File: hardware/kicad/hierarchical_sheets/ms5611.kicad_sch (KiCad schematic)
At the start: 3 parts, among them U4 MS5611-01BA

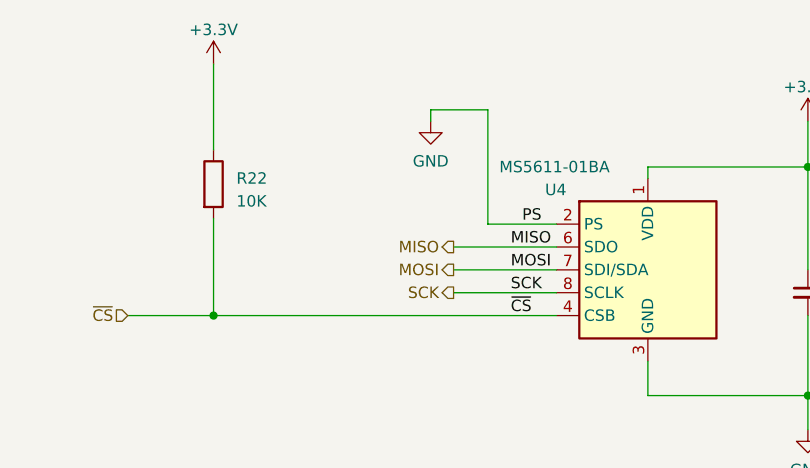
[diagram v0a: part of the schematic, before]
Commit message: assigned footprints
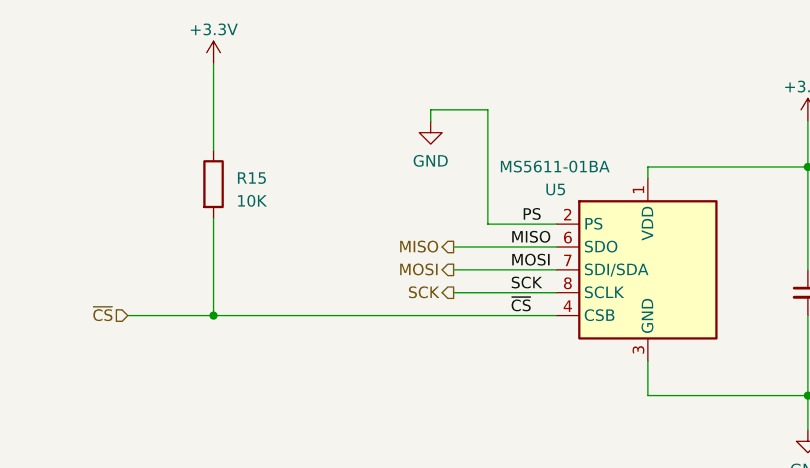
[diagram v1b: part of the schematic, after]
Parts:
- C6: footprint (none) -> Resistor_SMD:R_0603_1608Metric
- R15: renamed from R22; footprint (none) -> Resistor_SMD:R_0603_1608Metric
- U5: renamed from U4; Digikey https://www.digikey.com/en/products/detail/te-connectivity-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 -> (none)
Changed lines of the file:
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@@
         )
         (path "/54cce219-8b98-4e71-96c4-f9ee784aa3bc/01e59dc5-0a98-4437-b4f9-a1305517a629"
-          (reference "#PWR07") (unit 1)
+          (reference "#PWR024") (unit 1)
         )
       )
@@
   (symbol (lib_id "Device:R") (at 40.005 77.47 0) (unit 1)
     (in_bom yes) (on_board yes) (dnp no) (fields_autoplaced)
-    (property "Reference" "R22" (at 42.545 76.835 0)
+    (property "Reference" "R15" (at 42.545 76.835 0)
       (effects (font (size 1.27 1.27)) (justify left))
     )
@@
       (effects (font (size 1.27 1.27)) (justify left))
     )
-    (property "Footprint" "" (at 38.227 77.47 90)
+    (property "Footprint" "Resistor_SMD:R_0603_1608Metric" (at 38.227 77.47 90)
       (effects (font (size 1.27 1.27)) hide)
     )
@@
       (project "FC"
         (path "/54cce219-8b98-4e71-96c4-f9ee784aa3bc/01e59dc5-0a98-4437-b4f9-a1305517a629"
-          (reference "R22") (unit 1)
+          (reference "R15") (unit 1)
         )
       )
@@
         )
         (path "/54cce219-8b98-4e71-96c4-f9ee784aa3bc/01e59dc5-0a98-4437-b4f9-a1305517a629"
-          (reference "#PWR05") (unit 1)
+          (reference "#PWR023") (unit 1)
         )
       )
@@
   (symbol (lib_id "Sensor_Pressure:MS5611-01BA") (at 88.265 86.995 0) (unit 1)
     (in_bom yes) (on_board yes) (dnp no)
-    (property "Reference" "U4" (at 76.835 78.105 0)
+    (property "Reference" "U5" (at 76.835 78.105 0)
       (effects (font (size 1.27 1.27)) (justify left))
     )
@@
     )
     (property "Datasheet" "https://www.te.com/commerce/DocumentDelivery/DDEController?Action=srchrtrv&DocNm=MS5611-01BA03&DocType=Data+Sheet&DocLang=English" (at 88.265 86.995 0)
-      (effects (font (size 1.27 1.27)) hide)
-    )
-    (property "Digikey" "https://www.digikey.com/en/products/detail/te-connectivity-measurement-specialties/MS561101BA03-50/5277445" (at 88.265 86.995 0)
       (effects (font (size 1.27 1.27)) hide)
     )
@@
       (project "FC"
         (path "/54cce219-8b98-4e71-96c4-f9ee784aa3bc/01e59dc5-0a98-4437-b4f9-a1305517a629"
-          (reference "U4") (unit 1)
+          (reference "U5") (unit 1)
         )
       )
@@
         )
         (path "/54cce219-8b98-4e71-96c4-f9ee784aa3bc/01e59dc5-0a98-4437-b4f9-a1305517a629"
-          (reference "#PWR028") (unit 1)
+          (reference "#PWR021") (unit 1)
         )
       )
@@
       (effects (font (size 1.27 1.27)) (justify left))
     )
-    (property "Footprint" "" (at 106.045 89.535 0)
+    (property "Footprint" "Resistor_SMD:R_0603_1608Metric" (at 106.045 89.535 0)
       (effects (font (size 1.27 1.27)) hide)
     )

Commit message: making formatting more consistent
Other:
- moved on the sheet: C6, R15, U5

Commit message: formatting
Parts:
- renumbered U5 to U6
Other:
- title: SRAD-FC -> Barometer (MS5611)
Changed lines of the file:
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@@
   (paper "USLetter")
   (title_block
-    (title "SRAD-FC")
+    (title "Barometer (MS5611)")
     (company "Missouri S&T Rocket Design Team")
     (comment 1 "Ben Martin")
@@
   (symbol (lib_id "Sensor_Pressure:MS5611-01BA") (at 150.495 96.52 0) (unit 1)
     (in_bom yes) (on_board yes) (dnp no)
-    (property "Reference" "U5" (at 139.065 87.63 0)
-      (effects (font (size 1.27 1.27)) (justify left))
-    )
-    (property "Value" "MS5611-01BA" (at 133.985 85.09 0)
+    (property "Reference" "U6" (at 139.065 84.455 0)
+      (effects (font (size 1.27 1.27)) (justify left))
+    )
+    (property "Value" "MS5611-01BA" (at 133.985 86.36 0)
       (effects (font (size 1.27 1.27)) (justify left))
     )
@@
       (project "FC"
         (path "/54cce219-8b98-4e71-96c4-f9ee784aa3bc/01e59dc5-0a98-4437-b4f9-a1305517a629"
-          (reference "U5") (unit 1)
-        )
-      )
+          (reference "U6") (unit 1)
+        )
+      )

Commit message: finished routing
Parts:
- U6: Digikey (none) -> https://www.digikey.com/en/products/detail/te-connectivity-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
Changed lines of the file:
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@@
+      (effects (font (size 1.27 1.27)) hide)
+    )
+    (property "Digikey" "https://www.digikey.com/en/products/detail/te-connectivity-measurement-specialties/MS561101BA03-50/5277445" (at 150.495 96.52 0)
       (effects (font (size 1.27 1.27)) hide)
     )
